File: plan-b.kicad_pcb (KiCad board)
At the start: 4 copper layers, 16 x 42 mm, 68 parts, among them J1 HRO_TYPE-C-31-M-14, J2 Battery, J3 rgb, J4 columns, J5 Conn_01x10, J6 rows, J7 sensor, J8 Conn_ARM_SWD_TagConnect_TC203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, J9 Conn_01x05_Pin, J99 Net tie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

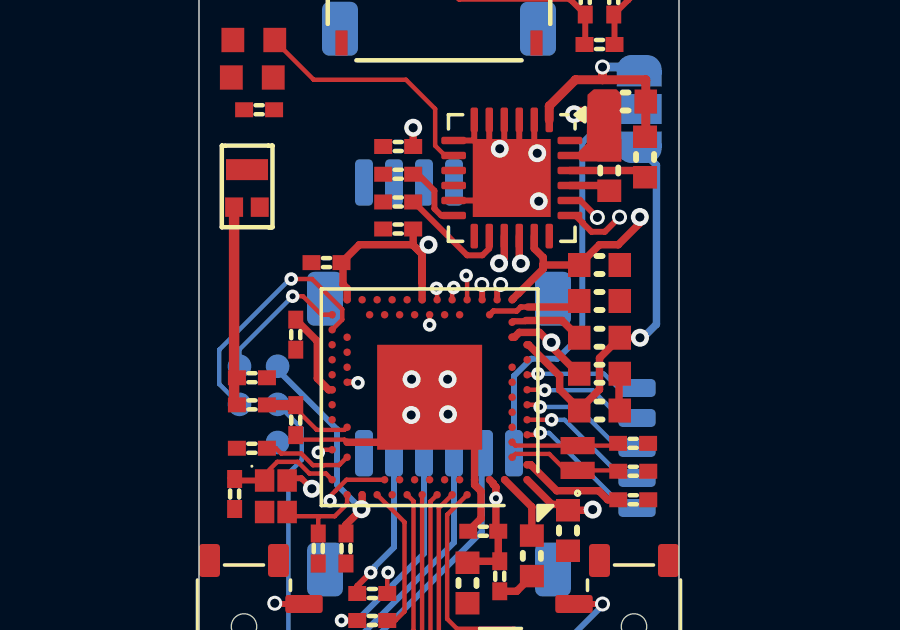
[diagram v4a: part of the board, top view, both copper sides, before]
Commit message: Wiring the columns socket
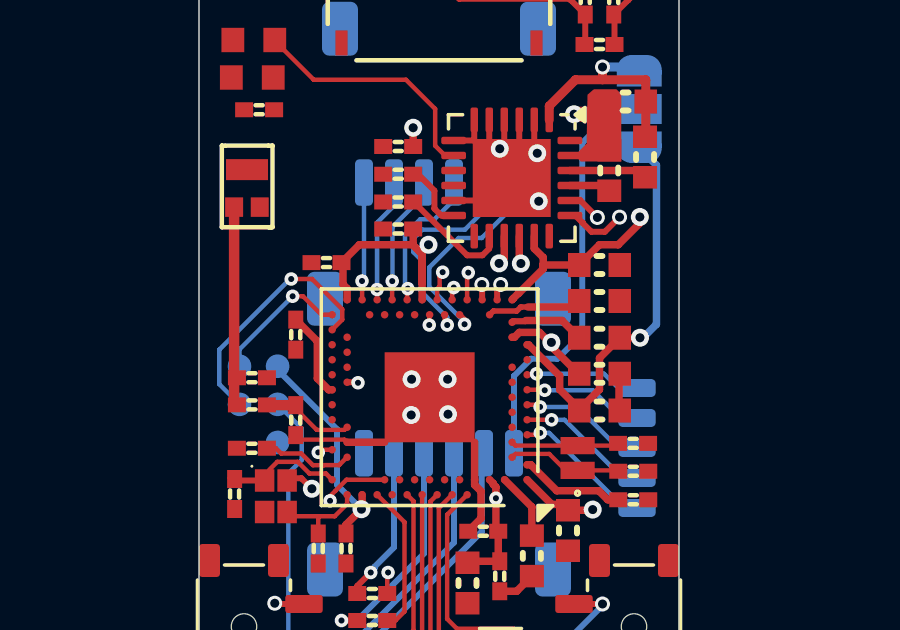
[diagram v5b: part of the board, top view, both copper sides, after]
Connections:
- U1 pad AC11: unconnected-(U1-P0.16-PadAC11) -> Col 1
- U1 pad AC9: unconnected-(U1-P0.14-PadAC9) -> Col 0
- U1 pad AD16: unconnected-(U1-P0.20-PadAD16) -> Col 2
- U1 pad AD18: unconnected-(U1-P0.22-PadAD18) -> Col 3
- U1 pad AD20: unconnected-(U1-P0.24-PadAD20) -> Col 4
- U1 pad AD22: unconnected-(U1-P1.00-PadAD22) -> Col 5
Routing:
- net D-: track 20.6 -> 41.4 mm
- net Col 1: track 0.00 -> 7.49 mm, vias 0 -> 1
- net Col 0: track 0.00 -> 7.23 mm, vias 0 -> 1
- net Col 2: track 0.00 -> 4.91 mm, vias 0 -> 1
- net Col 3: track 0.00 -> 4.35 mm, vias 0 -> 1
- net Col 4: track 0.00 -> 4.14 mm, vias 0 -> 1
- net Col 5: track 0.00 -> 3.94 mm, vias 0 -> 1
- net RST: track 48.5 -> 49.9 mm

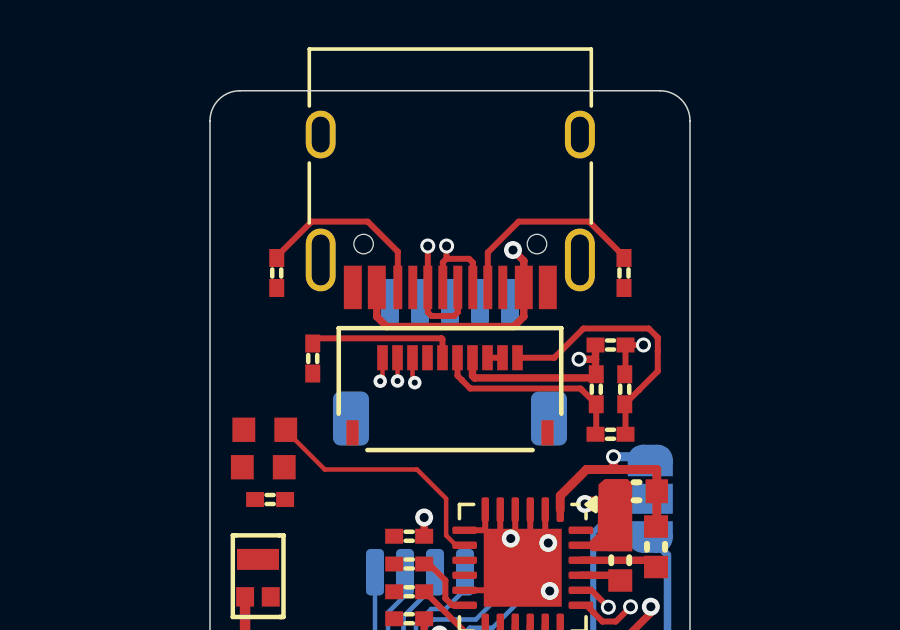
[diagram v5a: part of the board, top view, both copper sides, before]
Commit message: Swapping rows connector to the same 6 pins as columns
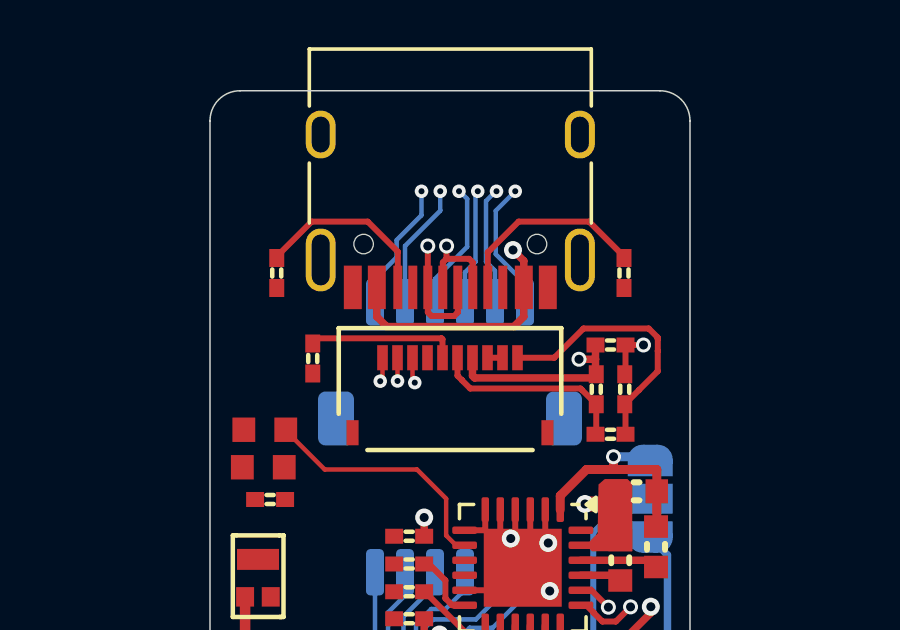
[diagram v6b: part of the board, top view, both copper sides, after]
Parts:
- J6: footprint Connector_JST:JST_SH_SM05B-SRSS-TB_1x05-1MP_P1.00mm_Horizontal -> Connector_JST:JST_SH_SM06B-SRSS-TB_1x06-1MP_P1.00mm_Horizontal
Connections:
- net LCD DATA renamed DATA
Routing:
- net Row 5: track 0.00 -> 4.39 mm, vias 0 -> 1
- net Row 0: track 0.00 -> 4.37 mm, vias 0 -> 1
- net Row 3: track 0.00 -> 4.31 mm, vias 0 -> 1
- net Row 4: track 0.00 -> 4.24 mm, vias 0 -> 1
- net Row 1: track 0.00 -> 4.03 mm, vias 0 -> 1
- net Row 2: track 0.00 -> 3.92 mm, vias 0 -> 1
- net RST: track 49.9 -> 48.9 mm

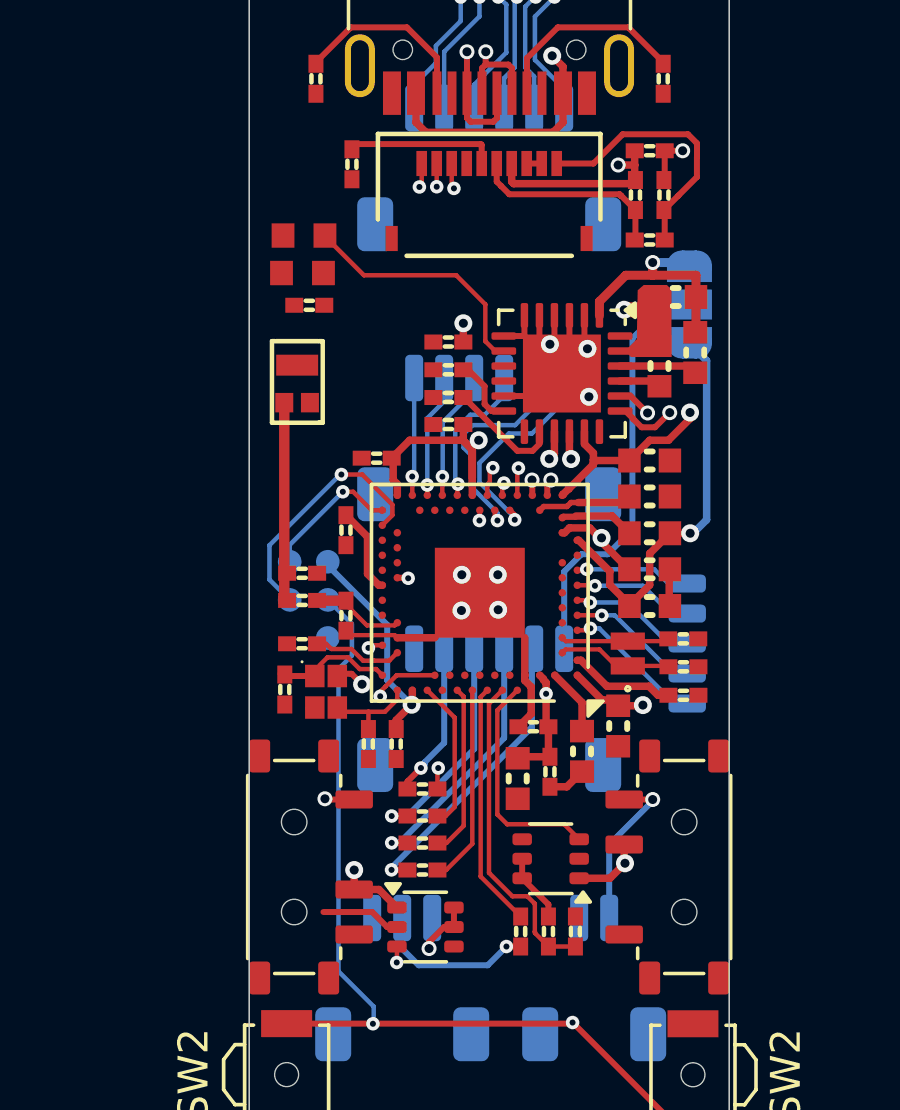
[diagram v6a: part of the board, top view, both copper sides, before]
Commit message: Wiring the rows connector to the MCU
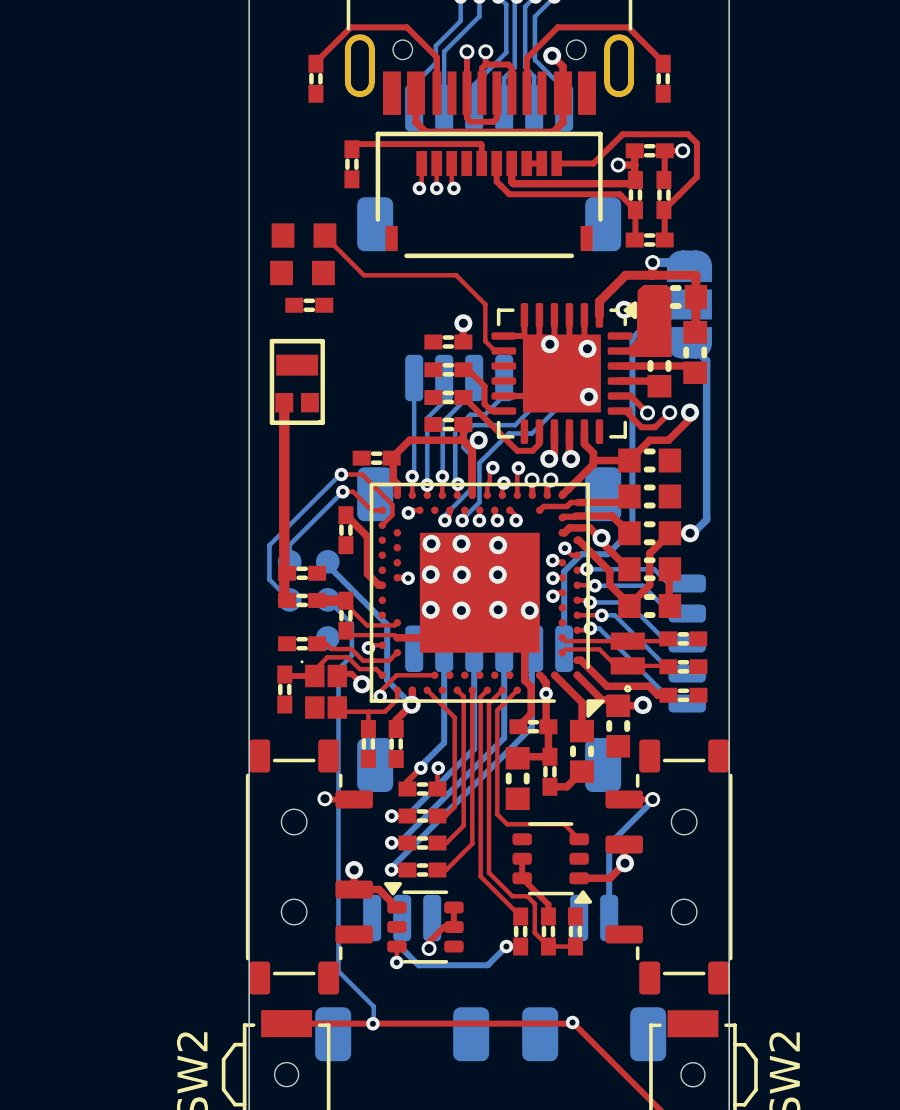
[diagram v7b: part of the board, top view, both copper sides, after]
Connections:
- U1 pad AC11: Col 1 -> Row 5
- U1 pad AC15: unconnected-(U1-P0.19-PadAC15) -> Col 0
- U1 pad AC17: unconnected-(U1-P0.21-PadAC17) -> Col 1
- U1 pad AC21: unconnected-(U1-P0.25-PadAC21) -> BLED
- U1 pad AC9: Col 0 -> Row 4
- U1 pad M2: unconnected-(U1-P0.07-PadM2) -> Row 3
- U1 pad P2: unconnected-(U1-P1.08-PadP2) -> Row 2
- U1 pad T2: unconnected-(U1-P0.11-PadT2) -> Row 1
- U1 pad U1: unconnected-(U1-P0.12-PadU1) -> Row 0
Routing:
- net Row 3: track 4.31 -> 27.5 mm, vias 1 -> 2
- net Row 2: track 3.92 -> 26.2 mm, vias 1 -> 2
- net Row 0: track 4.37 -> 26.5 mm, vias 1 -> 2
- net Row 1: track 4.03 -> 26.2 mm, vias 1 -> 2
- net Row 4: track 4.24 -> 24.6 mm, vias 1 -> 2
- net Row 5: track 4.39 -> 24.6 mm, vias 1 -> 2
- net GND: track 23.9 -> 21.3 mm, vias 9 -> 15
- net BLED: track 0.00 -> 0.42 mm, vias 0 -> 1

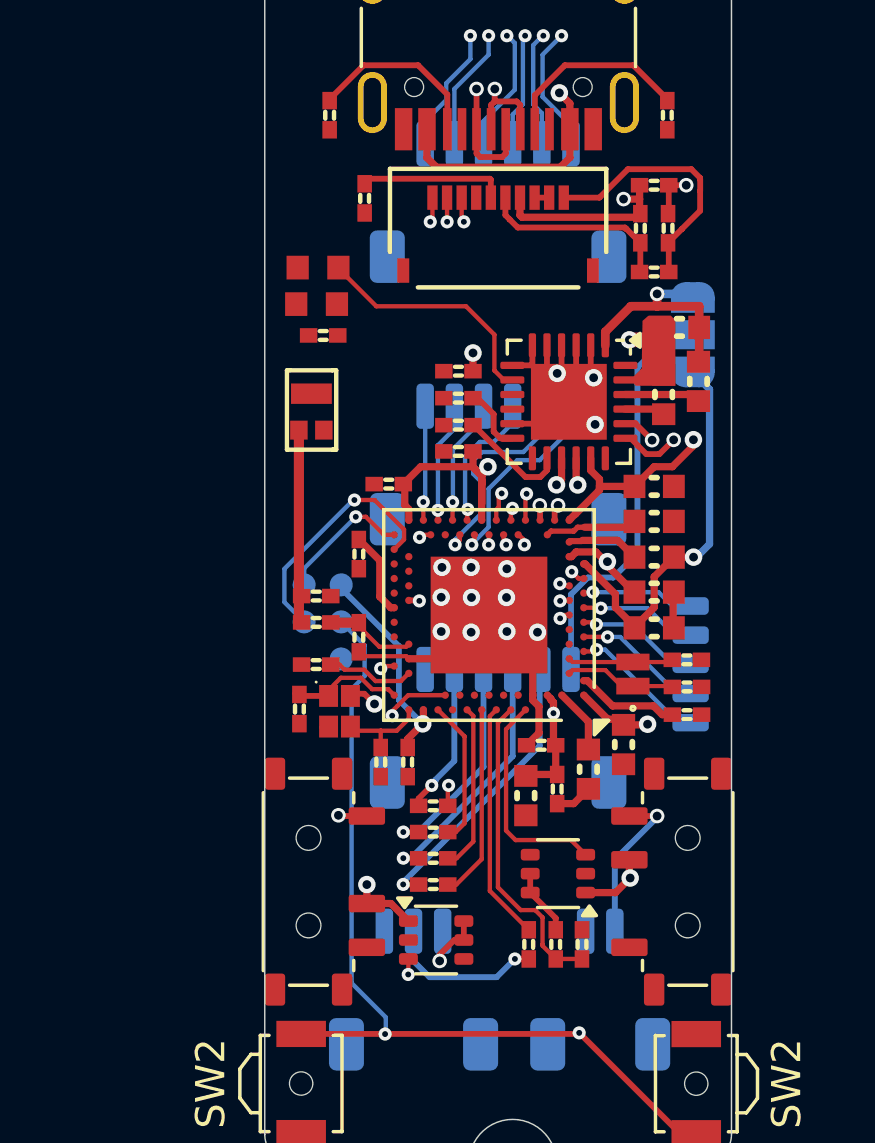
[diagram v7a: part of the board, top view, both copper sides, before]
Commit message: Connecting the status LEDs
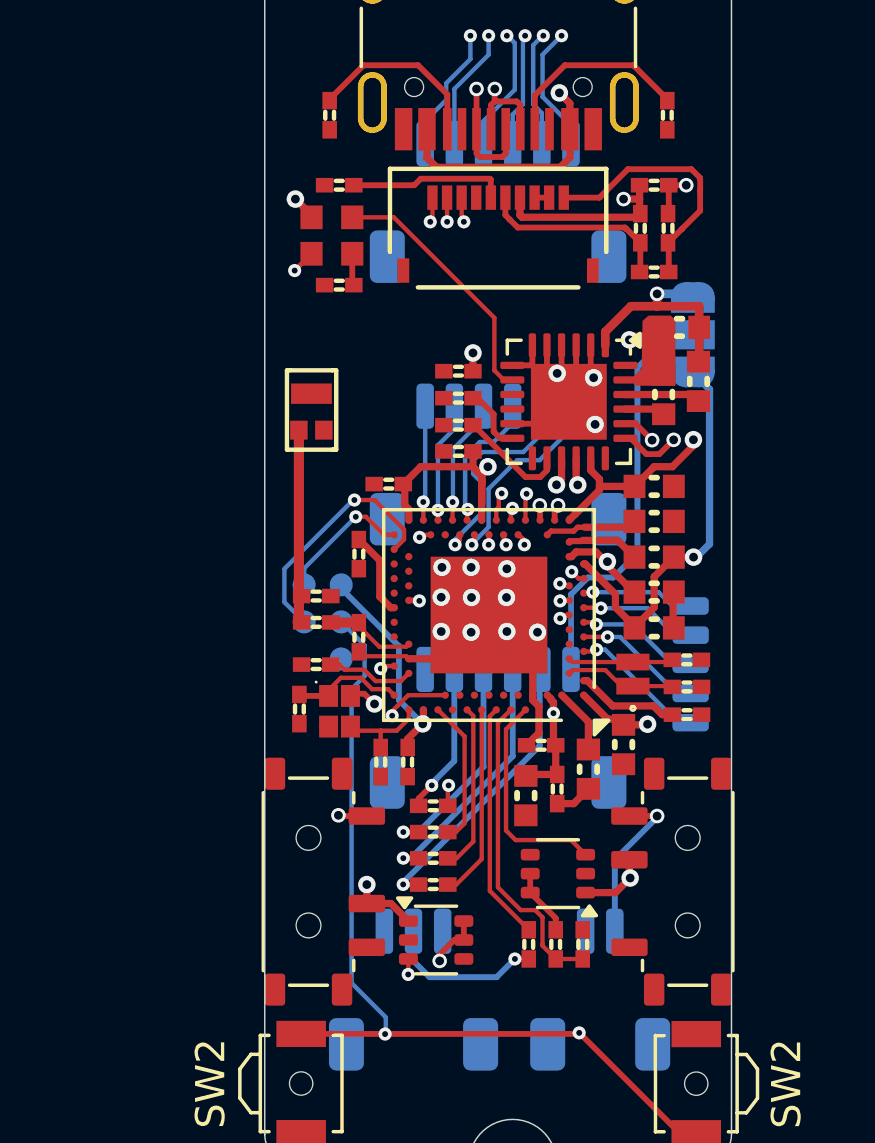
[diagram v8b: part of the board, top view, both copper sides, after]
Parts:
- moved R_BLE1 1.81 mm to (144.6, 69.6)
- moved LD3 1.80 mm to (144.3, 68.5)
- moved LD2 1.79 mm to (144.3, 67.2)
- moved C37 0.98 mm to (144.6, 66.1), turned to 180 degrees
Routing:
- net VSYS: track 7.14 -> 43.8 mm, vias 2 -> 3
- net BLED: track 0.42 -> 14.4 mm, vias 1 -> 2
- net VBAT: track 41.7 -> 38.9 mm
- net Net-(LD3-C): track 0.00 -> 1.10 mm
- net Net-(LD2-C): track 8.29 -> 8.85 mm
